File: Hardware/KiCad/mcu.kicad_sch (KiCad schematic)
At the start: 9 parts, among them U3 STM32F427ZGTx, Y1 8 MHz, Y2 32 kHz

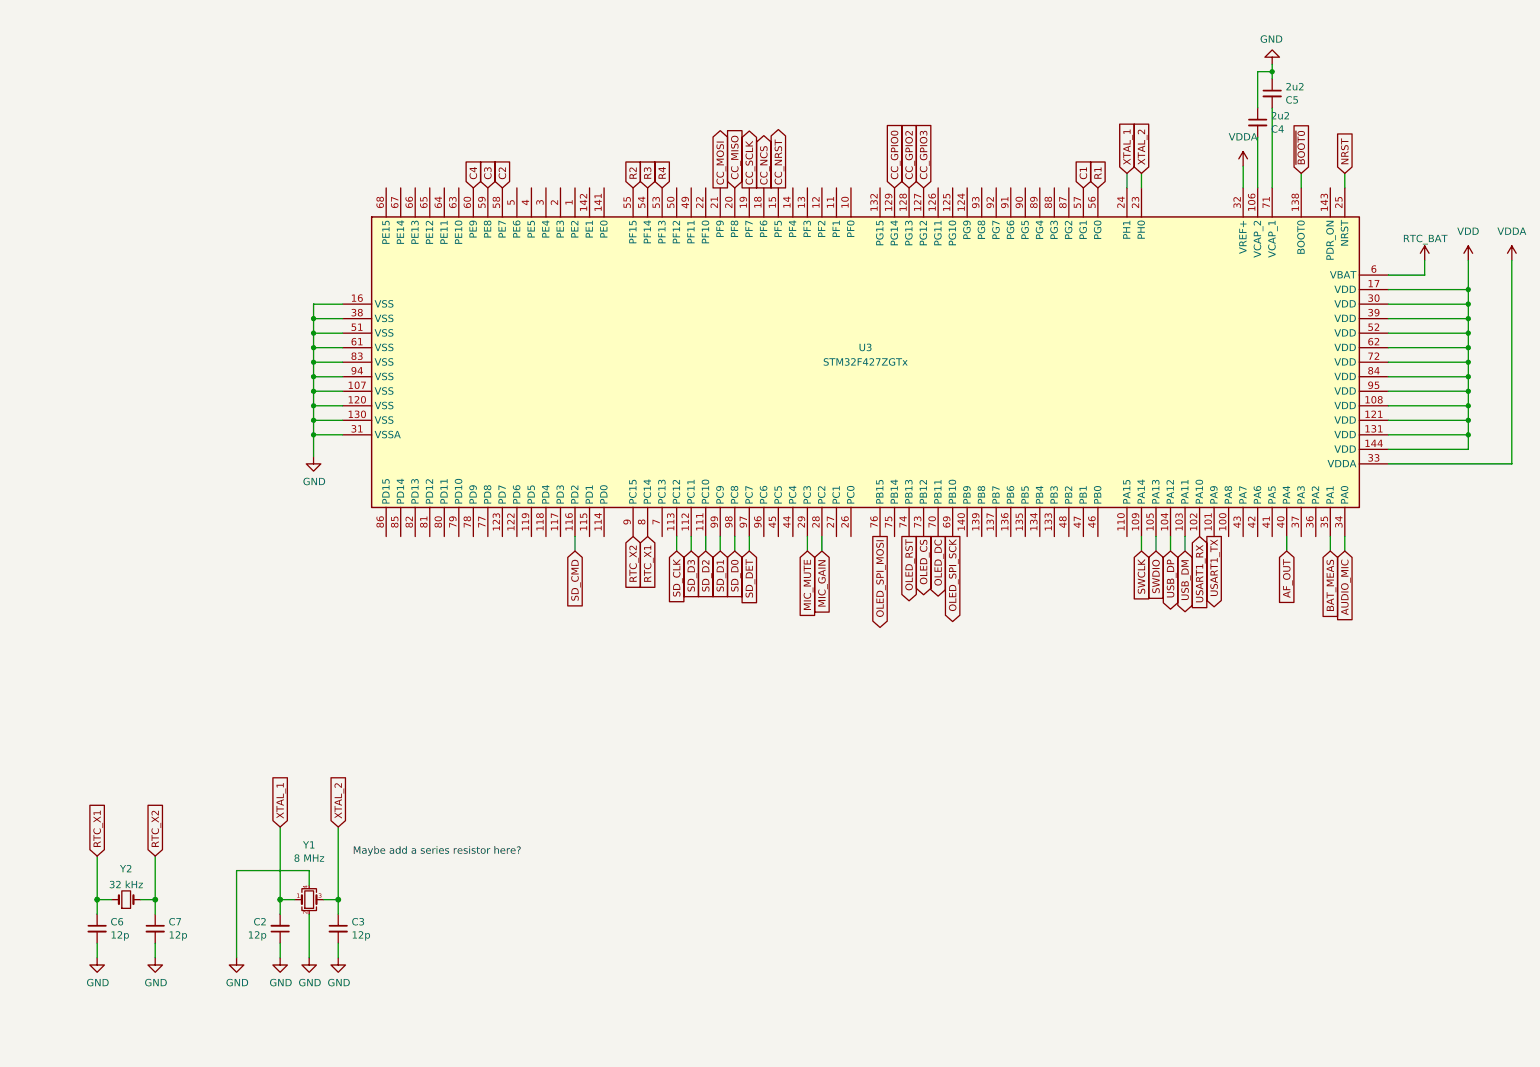
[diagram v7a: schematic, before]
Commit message: fix issue 21 & 20 & move MCU to align w/ grid
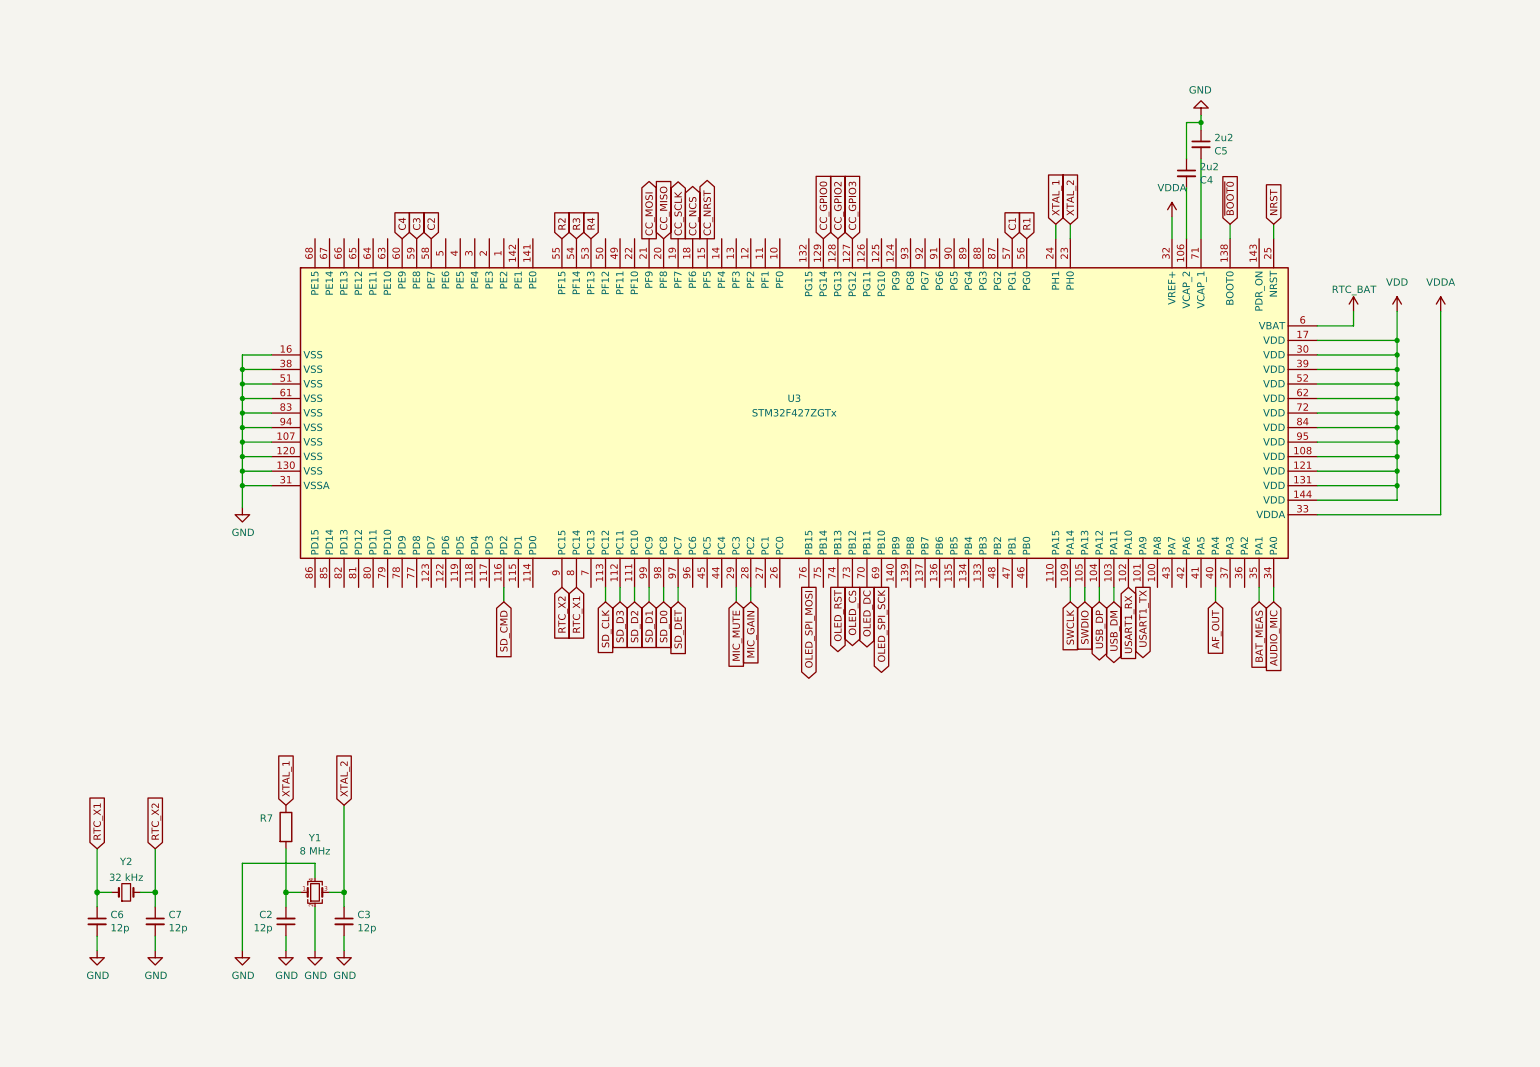
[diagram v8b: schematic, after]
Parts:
- added R7: (no value), symbol Device:R
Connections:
- net XTAL_1: now also R7.1; no longer C2.2, Y1.1
- new net: C2.2, R7.2, Y1.1
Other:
- note removed: "Maybe add a series resistor here?"
- moved on the sheet: C2, C3, C4, C5, C6, C7, U3, Y1, Y2
